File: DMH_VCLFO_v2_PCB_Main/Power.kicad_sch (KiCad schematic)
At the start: 20 parts, among them J0 Conn_01x01, J100 IDC_02x08, J300 Conn_01x08, U1 TL074, U2 TL074, U3 TL074

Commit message: Prepared for PCB design
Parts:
- removed D3, D4: LM4040LP-5, Package_TO_SOT_THT:TO-92_Inline, symbol Reference_Voltage:LM4040LP-5
- removed R1, R2: 6k8, Resistor_THT:R_Axial_DIN0207_L6.3mm_D2.5mm_P7.62mm_Horizontal, symbol Device:R_US
- J52: renamed from J300; value Conn_01x08 -> Conn_01x06; footprint Connector_PinHeader_2.54mm:PinHeader_1x08_P2.54mm_Vertical -> Connector_PinHeader_2.54mm:PinHeader_1x06_P2.54mm_Vertical; symbol Connector_Generic:Conn_01x08 -> Connector_Generic:Conn_01x06
- U1: footprint (none) -> Package_DIP:DIP-14_W7.62mm_Socket
- renumbered C1 to C55, C3 to C56, C23 to C57, C25 to C58, C2 to C59, C4 to C60, C24 to C61, C26 to C62, D2 to D25, D1 to D26, J0 to J53
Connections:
- net +5V is gone; now on net GND: J52.2 (Pin_2)
- net -12V: now also J52.6 (Pin_6); no longer J52.8 (Pin_8)
- net GND: no longer J52.6 (Pin_6)
- removed net -5V: J52.7 (Pin_7)
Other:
- note removed: "1mA"
- moved on the sheet: D25, D26, J100, J53

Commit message: Main PCB comp placement in progress
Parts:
- added J54: Conn_01x06, Connector_PinSocket_2.54mm:PinSocket_1x06_P2.54mm_Vertical, symbol Connector_Generic:Conn_01x06
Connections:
- net +12V: now also J54.1 (Pin_1)
- net -12V: now also J54.6 (Pin_6)
- net GND: now also J54.2 (Pin_2), J54.3 (Pin_3), J54.4 (Pin_4), J54.5 (Pin_5)
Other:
- moved on the sheet: J52

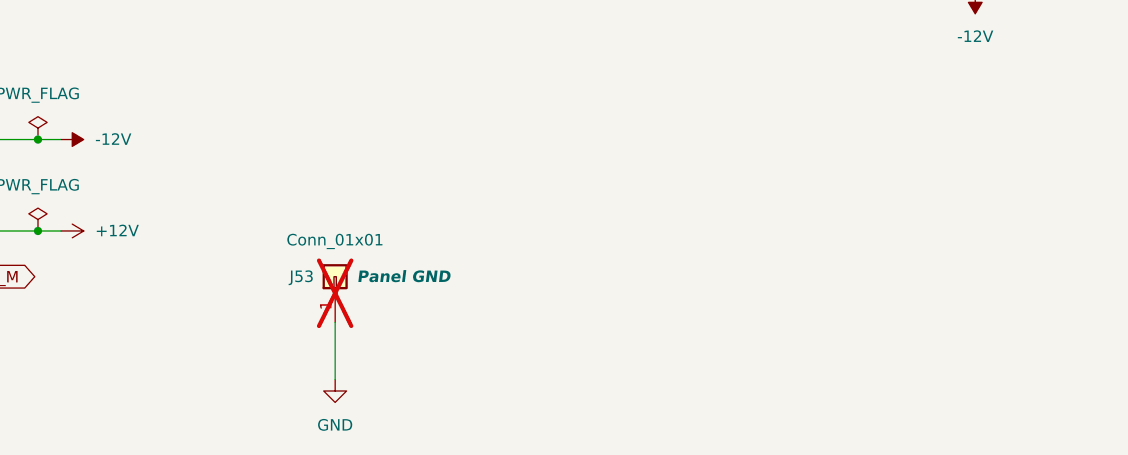
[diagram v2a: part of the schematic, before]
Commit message: Main PCB placement done
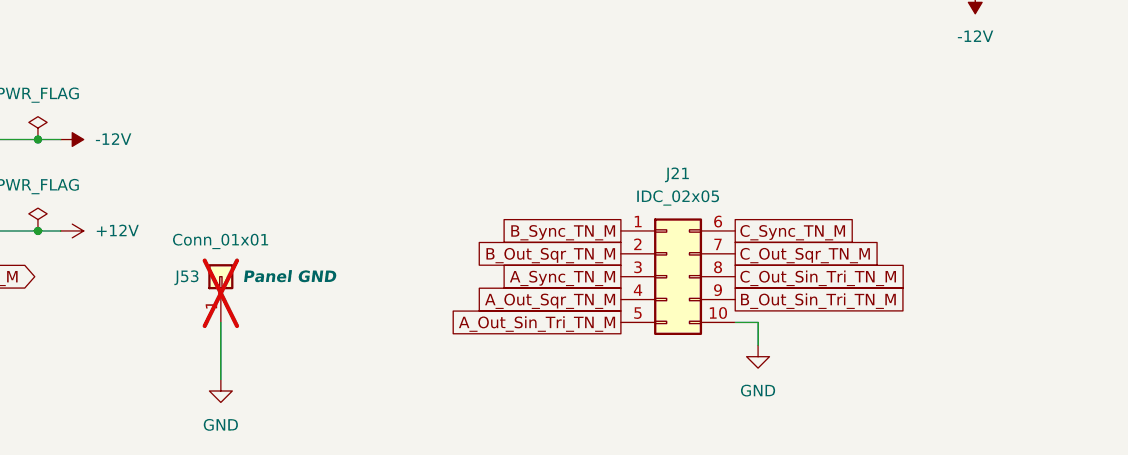
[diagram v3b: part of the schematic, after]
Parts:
- added J21: IDC_02x05, SynthStuff:IDC-Header_2x05_P2.54mm_Vertical_BackBone, symbol SynthStuff:BackBone_Connector_10Pin
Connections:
- net GND: now also J21.10 (Pin_10)
- new net A_Out_Sin_Tri_TN_M: J21.5 (Pin_5)
- new net A_Out_Sqr_TN_M: J21.4 (Pin_4)
- new net A_Sync_TN_M: J21.3 (Pin_3)
- new net B_Out_Sin_Tri_TN_M: J21.9 (Pin_9)
- new net B_Out_Sqr_TN_M: J21.2 (Pin_2)
- new net B_Sync_TN_M: J21.1 (Pin_1)
- new net C_Out_Sin_Tri_TN_M: J21.8 (Pin_8)
- new net C_Out_Sqr_TN_M: J21.7 (Pin_7)
- new net C_Sync_TN_M: J21.6 (Pin_6)
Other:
- moved on the sheet: J53

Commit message: Main PCB routing done
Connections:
- net GND: no longer J21.10 (Pin_10)
- no-connect marks 4 -> 5
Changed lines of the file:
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@@
+	)
+	(no_connect
+		(at 146.05 182.88)
 	)
 	(no_connect
@@
 	(wire
 		(pts
-			(xy 148.59 185.42) (xy 148.59 182.88)
-		)
-		(stroke
-			(width 0)
-			(type default)
-		)
-	)
-	(wire
-		(pts
 			(xy 196.85 125.73) (xy 196.85 123.19)
 		)
@@
 		(pts
 			(xy 88.9 95.25) (xy 101.6 95.25)
-		)
-		(stroke
-			(width 0)
-			(type default)
-		)
-	)
-	(wire
-		(pts
-			(xy 146.05 182.88) (xy 148.59 182.88)
 		)
 		(stroke
@@
 					(unit 1)
 				)
-			)
-		)
-	)
-	(symbol
-		(lib_id "power:GND")
-		(at 148.59 185.42 0)
-		(unit 1)
-		(exclude_from_sim no)
-		(in_bom yes)
-		(on_board yes)
-		(dnp no)
-		(fields_autoplaced yes)
-		(property "Reference" "#PWR018"
-			(at 148.59 191.77 0)
-			(effects
-				(font
-					(size 1.27 1.27)
-				)
-				(hide yes)
-			)
-		)
-		(property "Value" "GND"
-			(at 148.59 190.5 0)
-			(effects
-				(font
-					(size 1.27 1.27)
-				)
-			)
-		)
-		(property "Footprint" ""
-			(at 148.59 185.42 0)
-			(effects
-				(font
-					(size 1.27 1.27)
-				)
-				(hide yes)
-			)
-		)
-		(property "Datasheet" ""
-			(at 148.59 185.42 0)
-			(effects
-				(font
-					(size 1.27 1.27)
-				)
-				(hide yes)
-			)
-		)
-		(property "Description" "Power symbol creates a global label with name \"GND\" , ground"
-			(at 148.59 185.42 0)
-			(effects
-				(font
-					(size 1.27 1.27)
-				)
-				(hide yes)
-			)
-		)
-		(pin "1"
-		)
-		(instances
-			(project "DMH_VCLFO_v2_PCB_Main"
-				(path "/58f4306d-5387-4983-bb08-41a2313fd315/0cdf34b2-39cd-4d9e-981a-97cd34791509"
-					(reference "#PWR018")
-					(unit 1)
-				)
